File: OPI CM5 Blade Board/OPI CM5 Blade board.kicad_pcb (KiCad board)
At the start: 2 copper layers, 241.6 x 42.5 mm, 11 parts, among them J1 HIROSE_DF40C-100DS-0.4V_51_, J2 HIROSE_DF40C-100DS-0.4V_51_, J3 HIROSE_DF40C-100DS-0.4V_51_, J4 BUS_PCIexpress_x4, J5 M.2, U1 SHT4X, U5 SHT4X

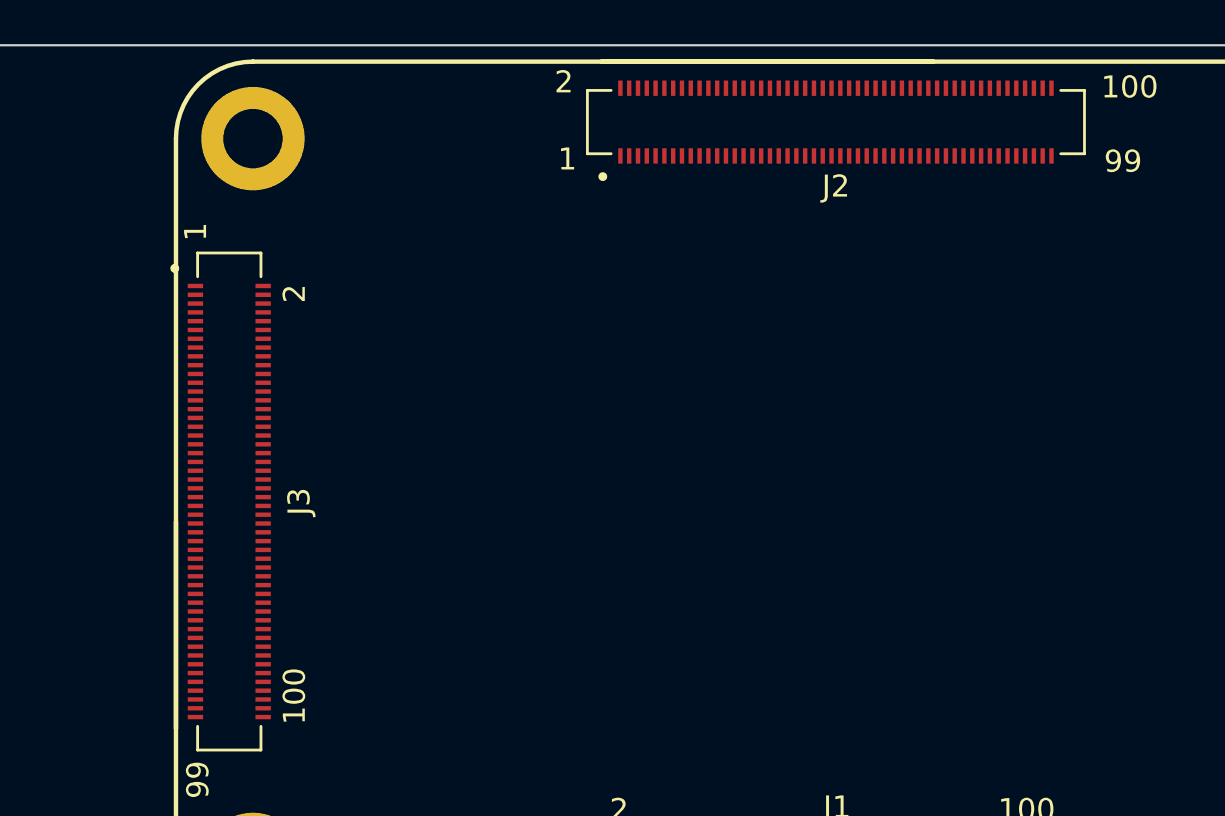
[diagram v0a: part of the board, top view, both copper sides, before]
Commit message: Working on HDMI PCIe connector wiring
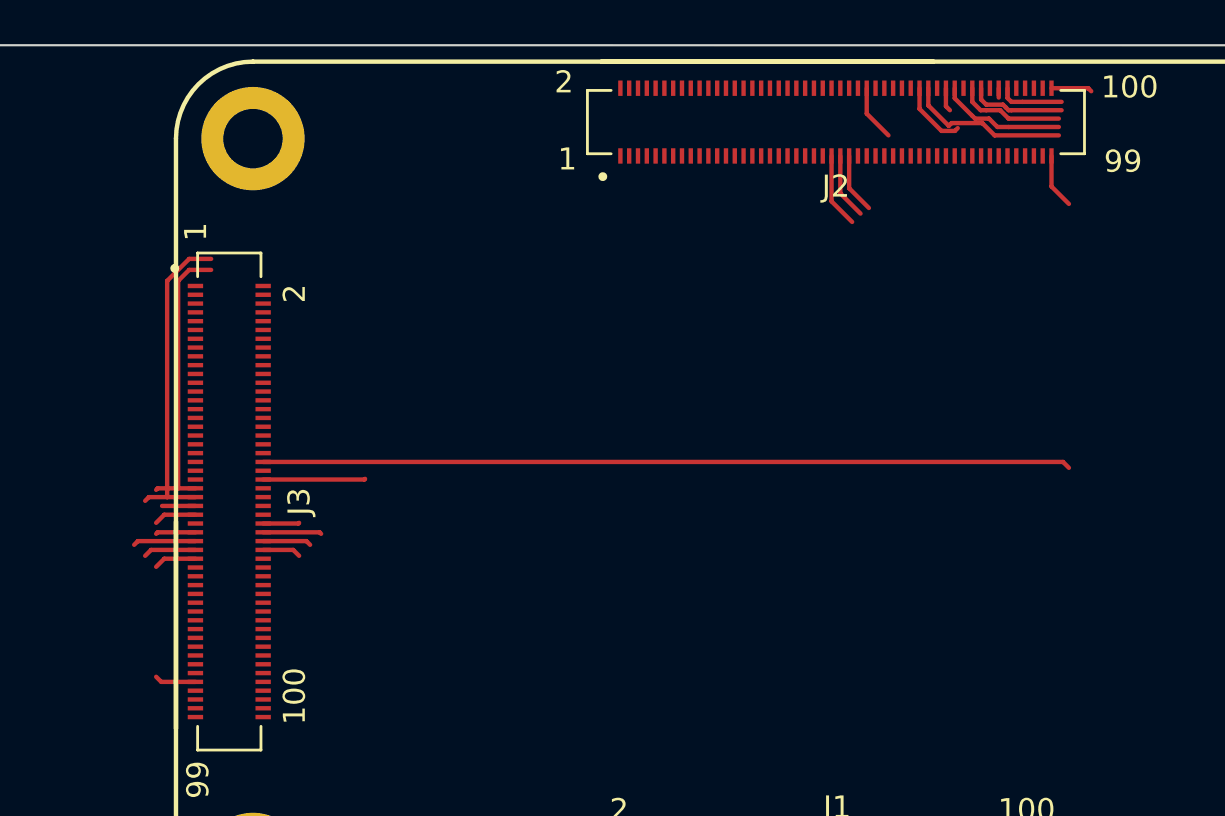
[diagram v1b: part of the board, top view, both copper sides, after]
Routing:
- net (no net): track 0.00 -> 137.6 mm
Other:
- copper layers 2 -> 4

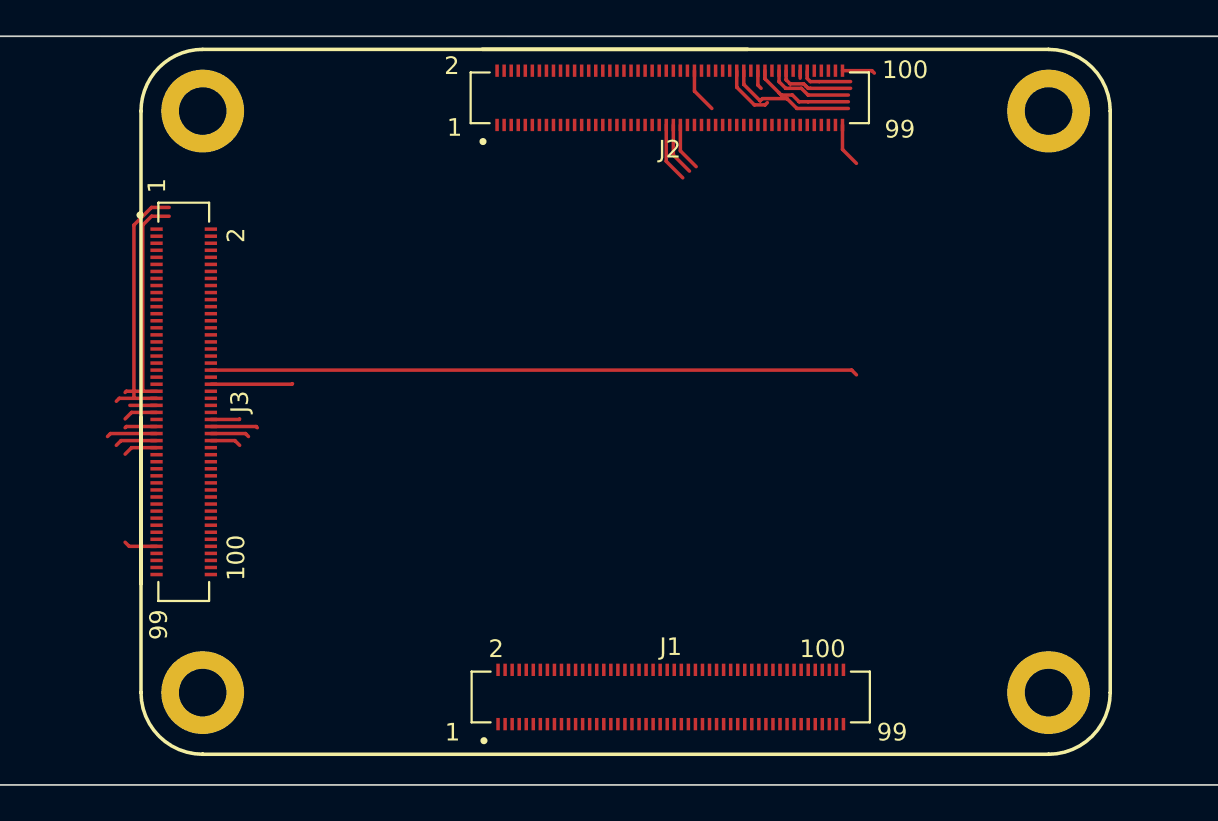
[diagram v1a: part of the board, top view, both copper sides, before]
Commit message: Working on USB differential pairs
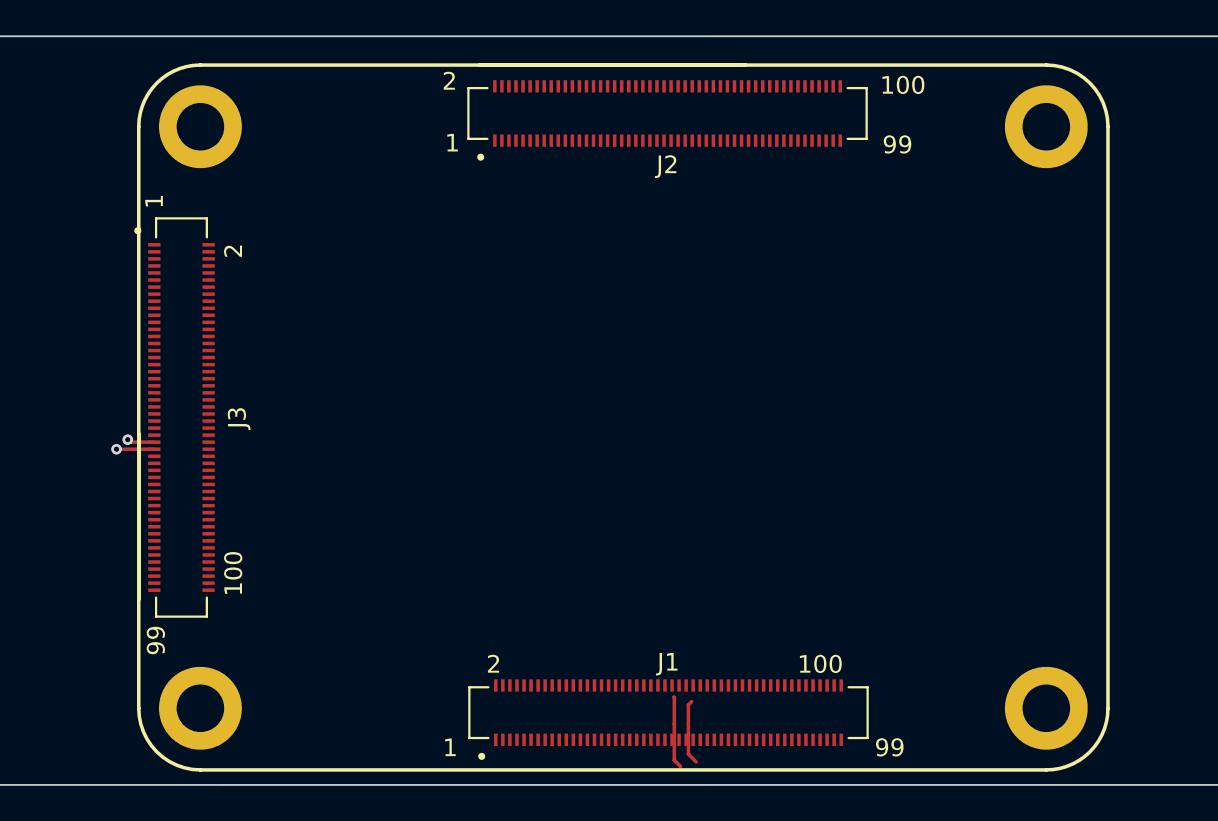
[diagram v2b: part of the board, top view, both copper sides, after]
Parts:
- moved H3 0.90 mm to (203.0, 33.3)
- moved H4 0.90 mm to (251.0, 33.3)
- moved J3 0.90 mm to (201.9, 49.8)
- moved H1 0.90 mm to (251.0, 66.3)
- moved H2 0.90 mm to (203.0, 66.3)
- moved J1 0.90 mm to (229.5, 66.5)
- moved J2 0.90 mm to (229.5, 32.5)
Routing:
- net (no net): track 137.6 -> 11.5 mm, vias 0 -> 2

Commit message: Working on M.2 SSD
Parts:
- removed U5: SHT4X, OPI_CM5_TEMP_SENSOR:SHT4X
- added D1: D5819WS, Diode_SMD:D_SOD-323, F.Cu at (174.8, 21.5)
- added D17: JEB05DFA, OPI_CM5_TVS_DIODE:DFN1006-2, F.Cu at (171.4, 18.1)
- added D2: JEB05DFA, OPI_CM5_TVS_DIODE:DFN1006-2, F.Cu at (171.4, 13.4)
- added D33: JEB05DFA, OPI_CM5_TVS_DIODE:DFN1006-2, F.Cu at (171.4, 20.5)
- added D4: JEB05DFA, OPI_CM5_TVS_DIODE:DFN1006-2, F.Cu at (171.4, 15.8)
- added ED5: ESD5341N, OPI_CM5_TVS_DIODE:DFN1006-2, F.Cu at (171.4, 22.8)
- added ED6: ESD5341N, OPI_CM5_TVS_DIODE:DFN1006-2, F.Cu at (171.4, 25.1)
- added Q1: 2SK3018, Package_TO_SOT_SMD:SOT-323_SC-70, F.Cu at (174.9, 14.3)
- added Q2: 2SK3018, Package_TO_SOT_SMD:SOT-323_SC-70, F.Cu at (174.9, 18.2)
- added U2: SHT40-BD1B-R3, OPI_CM5_TEMP_SENSOR:SHT4X, F.Cu at (174.4, 24.5)
- H1, H2, H3, H4: value MountingHole_2.7mm_M2.5_DIN965_Pad -> MountingHole_Pad
- J1: value HIROSE_DF40C-100DS-0.4V_51_ -> OPi_CM5_CORE JP1 100PIN
- J2: value HIROSE_DF40C-100DS-0.4V_51_ -> OPi_CM5_CORE JP2 100PIN
- J3: value HIROSE_DF40C-100DS-0.4V_51_ -> OPi_CM5_CORE JP13100PIN
- J4: value BUS_PCIexpress_x4 -> Bus_PCI_Express_x4
- J5: value M.2 -> J_1-2199230-5
- U1: value SHT4X -> SHT40-BD1B-R3
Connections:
- H1 pad 1: (no net) -> unconnected-(H1-Pad1)
- H2 pad 1: (no net) -> unconnected-(H2-Pad1)
- H3 pad 1: (no net) -> unconnected-(H3-Pad1)
- H4 pad 1: (no net) -> unconnected-(H4-Pad1)
- J1 pad 1: (no net) -> GND
- J1 pad 10: (no net) -> /Reserved
- J1 pad 100: (no net) -> /GPIO4_A5
- J1 pad 11: (no net) -> /Reserved
- J1 pad 12: (no net) -> /Reserved
- J1 pad 13: (no net) -> GND
- J1 pad 14: (no net) -> GND
- J1 pad 15: (no net) -> /Reserved
- J1 pad 16: (no net) -> /Reserved
- J1 pad 17: (no net) -> /Reserved
- J1 pad 18: (no net) -> /Reserved
- J1 pad 19: (no net) -> /Reserved
- J1 pad 2: (no net) -> GND
- J1 pad 20: (no net) -> /Reserved
- J1 pad 21: (no net) -> /GPIO4_A4
- J1 pad 22: (no net) -> GND
- J1 pad 23: (no net) -> GND
- J1 pad 24: (no net) -> /GPIO1_C0
- J1 pad 25: (no net) -> /GPIO1_B0
- J1 pad 26: (no net) -> /GPIO1_C1
- J1 pad 27: (no net) -> /GPIO1_B1
- J1 pad 28: (no net) -> /GPIO1_A2
- J1 pad 29: (no net) -> /GPIO1_B2
- J1 pad 3: (no net) -> /Reserved
- J1 pad 30: (no net) -> /GPIO1_A3
- J1 pad 31: (no net) -> /GPIO1_B3
- J1 pad 32: (no net) -> GND
- J1 pad 33: (no net) -> GND
- J1 pad 34: (no net) -> /GPIO1_A4
- J1 pad 35: (no net) -> /GPIO1_D6
- J1 pad 36: (no net) -> /GPIO1_D7
- J1 pad 37: (no net) -> /GPIO1_B4
- J1 pad 38: (no net) -> /GPIO1_A5
- J1 pad 39: (no net) -> /GPIO1_B5
- J1 pad 4: (no net) -> /Reserved
- J1 pad 40: (no net) -> /GPIO1_A6
- J1 pad 41: (no net) -> /GPIO1_B6
- J1 pad 42: (no net) -> GND
- J1 pad 43: (no net) -> GND
- J1 pad 44: (no net) -> /GPIO1_A7
- J1 pad 45: (no net) -> /GPIO1_B7
- J1 pad 46: (no net) -> /GPIO1_C4
- J1 pad 47: (no net) -> /GPIO0_C2
- J1 pad 48: (no net) -> /GPIO1_C6
- J1 pad 49: (no net) -> /GPIO1_D5
- J1 pad 5: (no net) -> /Reserved
- J1 pad 50: (no net) -> /GPIO1_D0
- J1 pad 51: (no net) -> /UART2_RX
- J1 pad 52: (no net) -> GND
- J1 pad 53: (no net) -> GND
- J1 pad 54: (no net) -> /GPIO1_D1
- J1 pad 55: (no net) -> /UART2_TX
- J1 pad 56: (no net) -> /GPIO1_D2
- J1 pad 57: (no net) -> /SDMMC_CLK
- J1 pad 58: (no net) -> /GPIO1_D3
- J1 pad 59: (no net) -> GND
- J1 pad 6: (no net) -> /Reserved
- J1 pad 60: (no net) -> GND
- J1 pad 61: (no net) -> /SDMMC_D3
- J1 pad 62: (no net) -> /SDMMC_CMD
- J1 pad 63: (no net) -> /SDMMC_D0
- J1 pad 64: (no net) -> /Reserved
- J1 pad 65: (no net) -> GND
- J1 pad 66: (no net) -> GND
- J1 pad 67: (no net) -> /SDMMC_D1
- J1 pad 68: (no net) -> /SARADC_IN1
- J1 pad 69: (no net) -> /SDMMC_D2
- J1 pad 7: (no net) -> GND
- J1 pad 70: (no net) -> /Reserved
- J1 pad 71: (no net) -> GND
- J1 pad 72: (no net) -> /Reserved
- J1 pad 73: (no net) -> /Reserved
- J1 pad 74: (no net) -> GND
- J1 pad 75: (no net) -> /SDMMC_PWREN
- J1 pad 76: (no net) -> /GPIO0_A4
- J1 pad 77: (no net) -> /VBUS
- J1 pad 78: (no net) -> /GPIO_VREF
- J1 pad 79: (no net) -> /VBUS
- J1 pad 8: (no net) -> GND
- J1 pad 80: (no net) -> /I2C6_SCL_M3
- J1 pad 81: (no net) -> /VBUS
- J1 pad 82: (no net) -> /I2C6_SDA_M3
- J1 pad 83: (no net) -> /VBUS
- J1 pad 84: (no net) -> /VCC_3V3_S3
- J1 pad 85: (no net) -> /VBUS
- J1 pad 86: (no net) -> /VCC_3V3_S3
- J1 pad 87: (no net) -> /VBUS
- J1 pad 88: (no net) -> /VCC_1V8_S3
- J1 pad 89: (no net) -> /Reserved
- J1 pad 9: (no net) -> /Reserved
- J1 pad 90: (no net) -> /VCC_1V8_S3
- J1 pad 91: (no net) -> /Reserved
- J1 pad 92: (no net) -> /PMIC_RESET_L
- J1 pad 93: (no net) -> /SARADC_IN0
- J1 pad 94: (no net) -> /SARADC_IN3
- J1 pad 95: (no net) -> /GPIO4_B6
- J1 pad 96: (no net) -> /SARADC_IN2
- J1 pad 97: (no net) -> /GPIO4_A7
- J1 pad 98: (no net) -> GND
- J1 pad 99: (no net) -> /PWRON_L
- J2 pad 1: (no net) -> /TYPEC0_USB20_OTG_ID
- J2 pad 10: (no net) -> /PCIE20_2_REFCLKP
- J2 pad 100: (no net) -> /HDMI_TX0_SCL_M0
- J2 pad 11: (no net) -> /Reserved
- J2 pad 12: (no net) -> /PCIE20_2_REFCLKN
- J2 pad 13: (no net) -> GND
- J2 pad 14: (no net) -> GND
- J2 pad 15: (no net) -> /MIPI_CSI0_D0N
- J2 pad 16: (no net) -> /PCIE20_2_RXP/SATA30_2_RXP
- J2 pad 17: (no net) -> /MIPI_CSI0_D0P
- J2 pad 18: (no net) -> /PCIE20_2_RXN/SATA30_2_RXN
- J2 pad 19: (no net) -> GND
- J2 pad 2: (no net) -> /GPIO1_A0
- J2 pad 20: (no net) -> GND
- J2 pad 21: (no net) -> /MIPI_CSI0_D1N
- J2 pad 22: (no net) -> /PCIE20_2_TXP/SATA30_2_TXP
- J2 pad 23: (no net) -> /MIPI_CSI0_D1P
- J2 pad 24: (no net) -> /PCIE20_2_TXN/SATA30_2_TXN
- J2 pad 25: (no net) -> GND
- J2 pad 26: (no net) -> GND
- J2 pad 27: (no net) -> /MIPI_CSI0_CLK0N
- J2 pad 28: (no net) -> /MIPI_DPHY0_RX_D0N
- J2 pad 29: (no net) -> /MIPI_CSI0_CLK0P
- J2 pad 3: (no net) -> /TYPEC0_USB20_OTG_DM
- J2 pad 30: (no net) -> /MIPI_DPHY0_RX_D0P
- J2 pad 31: (no net) -> GND
- J2 pad 32: (no net) -> GND
- J2 pad 33: (no net) -> /MIPI_CSI0_D2N
- J2 pad 34: (no net) -> /MIPI_DPHY0_RX_D1N
- J2 pad 35: (no net) -> /MIPI_CSI0_D2N
- J2 pad 36: (no net) -> /MIPI_DPHY0_RX_D1P
- J2 pad 37: (no net) -> GND
- J2 pad 38: (no net) -> GND
- J2 pad 39: (no net) -> /MIPI_CSI0_D3N
- J2 pad 4: (no net) -> /GPIO1_A1
- J2 pad 40: (no net) -> /MIPI_DPHY0_RX_CLKN
- J2 pad 41: (no net) -> /MIPI_CSI0_D3P
- J2 pad 42: (no net) -> /MIPI_DPHY0_RX_CLKP
- J2 pad 43: (no net) -> GND
- J2 pad 44: (no net) -> GND
- J2 pad 45: (no net) -> /MIPI_CSI0_CLK1N
- J2 pad 46: (no net) -> /Reserved
- J2 pad 47: (no net) -> /MIPI_CSI0_CLK1P
- J2 pad 48: (no net) -> /Reserved
- J2 pad 49: (no net) -> /HDMI0_TX_ON_H
- J2 pad 5: (no net) -> /TYPEC0_USB20_OTG_DP
- J2 pad 50: (no net) -> GND
- J2 pad 51: (no net) -> /HDMI_TX0_CEC_M0
- J2 pad 52: (no net) -> /Reserved
- J2 pad 53: (no net) -> /HDMI_TX0_SBDN
- J2 pad 54: (no net) -> /Reserved
- J2 pad 55: (no net) -> GND
- J2 pad 56: (no net) -> GND
- J2 pad 57: (no net) -> /MIPI_DPHY0_TX_D0N
- J2 pad 58: (no net) -> /HDMI0_SBDP
- J2 pad 59: (no net) -> /MIPI_DPHY0_TX_D0P
- J2 pad 6: (no net) -> /GPIO4_A6
- J2 pad 60: (no net) -> /Reserved
- J2 pad 61: (no net) -> GND
- J2 pad 62: (no net) -> GND
- J2 pad 63: (no net) -> /MIPI_DPHY0_TX_D1N
- J2 pad 64: (no net) -> /Reserved
- J2 pad 65: (no net) -> /MIPI_DPHY0_TX_D1P
- J2 pad 66: (no net) -> /Reserved
- J2 pad 67: (no net) -> GND
- J2 pad 68: (no net) -> GND
- J2 pad 69: (no net) -> /MIPI_DPHY0_TX_CLKN
- J2 pad 7: (no net) -> GND
- J2 pad 70: (no net) -> /HDMI_TX0_D2P
- J2 pad 71: (no net) -> /MIPI_DPHY0_TX_CLKP
- J2 pad 72: (no net) -> /HDMI_TX0_D2N
- J2 pad 73: (no net) -> GND
- J2 pad 74: (no net) -> GND
- J2 pad 75: (no net) -> /MIPI_DPHY1_TX_D0N
- J2 pad 76: (no net) -> /HDMI_TX0_D1P
- J2 pad 77: (no net) -> /MIPI_DPHY1_TX_D0P
- J2 pad 78: (no net) -> /HDMI_TX0_D1N
- J2 pad 79: (no net) -> GND
- J2 pad 8: (no net) -> GND
- J2 pad 80: (no net) -> GND
- J2 pad 81: (no net) -> /MIPI_DPHY1_TX_D1N
- J2 pad 82: (no net) -> /HDMI_TX0_D0P
- J2 pad 83: (no net) -> /MIPI_DPHY1_TX_D1P
- J2 pad 84: (no net) -> /HDMI_TX0_D0N
- J2 pad 85: (no net) -> GND
- J2 pad 86: (no net) -> GND
- J2 pad 87: (no net) -> /MIPI_DPHY1_TX_CLKN
- J2 pad 88: (no net) -> /HDMI_TX0_D3P
- J2 pad 89: (no net) -> /MIPI_DPHY1_TX_CLKP
- J2 pad 9: (no net) -> /GPIO4_A2
- J2 pad 90: (no net) -> /HDMI_TX0_D3N
- J2 pad 91: (no net) -> GND
- J2 pad 92: (no net) -> GND
- J2 pad 93: (no net) -> /MIPI_DPHY1_TX_D2N
- J2 pad 94: (no net) -> /MIPI_DPHY1_TX_D3N
- J2 pad 95: (no net) -> /MIPI_DPHY1_TX_D2P
- J2 pad 96: (no net) -> /MIPI_DPHY1_TX_D3P
- J2 pad 97: (no net) -> GND
- J2 pad 98: (no net) -> GND
- J2 pad 99: (no net) -> /HDMI_TX0_SDA_M0
- J3 pad 1: (no net) -> /USB20_HOST1_DP
- J3 pad 10: (no net) -> /TYPEC0_SSRX2N
- J3 pad 100: (no net) -> GND
- J3 pad 11: (no net) -> GND
- J3 pad 12: (no net) -> GND
- J3 pad 13: (no net) -> /USB20_HOST0_DP
- J3 pad 14: (no net) -> /TYPEC0_SSTX1N
- J3 pad 15: (no net) -> /USB20_HOST0_DM
- J3 pad 16: (no net) -> /TYPEC0_SSTX1P
- J3 pad 17: (no net) -> GND
- J3 pad 18: (no net) -> GND
- J3 pad 19: (no net) -> /TYPEC0_SSRX1P
- J3 pad 2: (no net) -> /TYPEC0_SSTX2P
- J3 pad 20: (no net) -> /GPIO3_C6
- J3 pad 21: (no net) -> /TYPEC0_SSRX1P
- J3 pad 22: (no net) -> /PCIE20x1_2_CLKREQn_M0
- J3 pad 23: (no net) -> GND
- J3 pad 24: (no net) -> /PCIE20x1_2_PERSTn_M0
- J3 pad 25: (no net) -> /MIPI_DPHY1_RX_CLKP
- J3 pad 26: (no net) -> /GPIO3_D5
- J3 pad 27: (no net) -> /MIPI_DPHY1_RX_CLKN
- J3 pad 28: (no net) -> /GPIO3_D2
- J3 pad 29: (no net) -> GND
- J3 pad 3: (no net) -> /USB20_HOST1_DN
- J3 pad 30: (no net) -> /GPIO3_D4
- J3 pad 31: (no net) -> /MIPI_DPHY1_RX_D1P
- J3 pad 32: (no net) -> GND
- J3 pad 33: (no net) -> /MIPI_DPHY1_RX_D1N
- J3 pad 34: (no net) -> /GPIO3_B7
- J3 pad 35: (no net) -> GND
- J3 pad 36: (no net) -> /GPIO3_C5
- J3 pad 37: (no net) -> /MIPI_DPHY1_RX_D0P
- J3 pad 38: (no net) -> /GPIO3_C4
- J3 pad 39: (no net) -> /MIPI_DPHY1_RX_D0N
- J3 pad 4: (no net) -> /TYPEC0_SSTX2N
- J3 pad 40: (no net) -> /GPIO3_D3
- J3 pad 41: (no net) -> GND
- J3 pad 42: (no net) -> /GMAC_TXD3
- J3 pad 43: (no net) -> /PCIE20x1_2_WAKEn_M0
- J3 pad 44: (no net) -> GND
- J3 pad 45: (no net) -> GND
- J3 pad 46: (no net) -> /GMAC_TXD0
- J3 pad 47: (no net) -> /GMAC_TXD2
- J3 pad 48: (no net) -> /GPIO3_B2
- J3 pad 49: (no net) -> /GMAC_TXD1
- J3 pad 5: (no net) -> GND
- J3 pad 50: (no net) -> /GPIO3_C1
- J3 pad 51: (no net) -> /GMAC_TXEN
- J3 pad 52: (no net) -> /GPIO3_A6
- J3 pad 53: (no net) -> /GMAC_MDIO
- J3 pad 54: (no net) -> GND
- J3 pad 55: (no net) -> GND
- J3 pad 56: (no net) -> /GMAC_RXD1
- J3 pad 57: (no net) -> /GMAC_MCLK/PWM13
- J3 pad 58: (no net) -> /GMAC_RXCLK
- J3 pad 59: (no net) -> /GMAC_RXDV
- J3 pad 6: (no net) -> GND
- J3 pad 60: (no net) -> /GMAC_RXD0
- J3 pad 61: (no net) -> /GMAC_RXD2
- J3 pad 62: (no net) -> /GMAC_TXCLK
- J3 pad 63: (no net) -> /GMAC_RXD3
- J3 pad 64: (no net) -> GND
- J3 pad 65: (no net) -> GND
- J3 pad 66: (no net) -> /GPIO0_B0
- J3 pad 67: (no net) -> /GPIO0_A0
- J3 pad 68: (no net) -> /I2S0_MCLK
- J3 pad 69: (no net) -> /GPIO1_C2
- J3 pad 7: (no net) -> /TYPEC0_SBU1
- J3 pad 70: (no net) -> /I2S0_SDO0
- J3 pad 71: (no net) -> /GPIO1_C5
- J3 pad 72: (no net) -> /GPIO3_C0
- J3 pad 73: (no net) -> /GPIO1_D4
- J3 pad 74: (no net) -> GND
- J3 pad 75: (no net) -> GND
- J3 pad 76: (no net) -> /PCIE20_0_REFCLKP
- J3 pad 77: (no net) -> /GPIO0_D5
- J3 pad 78: (no net) -> /PCIE20_0_REFCLKN
- J3 pad 79: (no net) -> /GPIO0_C7
- J3 pad 8: (no net) -> /TYPEC0_SSRX2P
- J3 pad 80: (no net) -> GND
- J3 pad 81: (no net) -> /GPIO0_D4
- J3 pad 82: (no net) -> /PCIE20_0_TXP
- J3 pad 83: (no net) -> /GPIO0_C4
- J3 pad 84: (no net) -> /PCIE20_0_TXN
- J3 pad 85: (no net) -> /GPIO0_D3
- J3 pad 86: (no net) -> GND
- J3 pad 87: (no net) -> GND
- J3 pad 88: (no net) -> /PCIE20_0_RXN
- J3 pad 89: (no net) -> /GPIO0_D0
- J3 pad 9: (no net) -> /TYPEC0_SBU2
- J3 pad 90: (no net) -> /PCIE20_0_RXP
- J3 pad 91: (no net) -> /GMAC_MDC
- J3 pad 92: (no net) -> GND
- J3 pad 93: (no net) -> /GPIO4_A3
- J3 pad 94: (no net) -> /GPIO0_C5
- J3 pad 95: (no net) -> /GPIO4_B3
- J3 pad 96: (no net) -> /GPIO0_B2
- J3 pad 97: (no net) -> /GPIO4_B2
- J3 pad 98: (no net) -> /GPIO0_C6
- J3 pad 99: (no net) -> GND
- J4 pad A1: (no net) -> unconnected-(J4-~{PRSNT1}-PadA1)
- J4 pad A10: (no net) -> Net-(J4-+3.3V-PadA10)
- J4 pad A11: (no net) -> unconnected-(J4-~{PERST}-PadA11)
- J4 pad A12: (no net) -> Net-(J4-GND-PadA12)
- J4 pad A13: (no net) -> unconnected-(J4-REFCLK+-PadA13)
- J4 pad A14: (no net) -> unconnected-(J4-REFCLK--PadA14)
- J4 pad A15: (no net) -> Net-(J4-GND-PadA12)
- J4 pad A16: (no net) -> unconnected-(J4-PERp0-PadA16)
- J4 pad A17: (no net) -> unconnected-(J4-PERn0-PadA17)
- J4 pad A18: (no net) -> Net-(J4-GND-PadA12)
- J4 pad A19: (no net) -> unconnected-(J4-RSVD-PadA19)
- J4 pad A2: (no net) -> Net-(J4-+12V-PadA2)
- J4 pad A20: (no net) -> Net-(J4-GND-PadA12)
- J4 pad A21: (no net) -> unconnected-(J4-PERp1-PadA21)
- J4 pad A22: (no net) -> unconnected-(J4-PERn1-PadA22)
- J4 pad A23: (no net) -> Net-(J4-GND-PadA12)
- J4 pad A24: (no net) -> Net-(J4-GND-PadA12)
- J4 pad A25: (no net) -> unconnected-(J4-PERp2-PadA25)
- J4 pad A26: (no net) -> unconnected-(J4-PERn2-PadA26)
- J4 pad A27: (no net) -> Net-(J4-GND-PadA12)
- J4 pad A28: (no net) -> Net-(J4-GND-PadA12)
- J4 pad A29: (no net) -> unconnected-(J4-PERp3-PadA29)
- J4 pad A3: (no net) -> Net-(J4-+12V-PadA2)
- J4 pad A30: (no net) -> unconnected-(J4-PERn3-PadA30)
- J4 pad A31: (no net) -> Net-(J4-GND-PadA12)
- J4 pad A32: (no net) -> unconnected-(J4-RSVD-PadA32)
- J4 pad A4: (no net) -> Net-(J4-GND-PadA12)
- J4 pad A5: (no net) -> unconnected-(J4-JTAG2-PadA5)
- J4 pad A6: (no net) -> unconnected-(J4-JTAG3-PadA6)
- J4 pad A7: (no net) -> unconnected-(J4-JTAG4-PadA7)
- J4 pad A8: (no net) -> unconnected-(J4-JTAG5-PadA8)
- J4 pad A9: (no net) -> Net-(J4-+3.3V-PadA10)
- J4 pad B1: (no net) -> Net-(J4-+12V-PadA2)
- J4 pad B10: (no net) -> unconnected-(J4-3.3Vaux-PadB10)
- J4 pad B11: (no net) -> unconnected-(J4-~{WAKE}-PadB11)
- J4 pad B12: (no net) -> unconnected-(J4-RSVD-PadB12)
- J4 pad B13: (no net) -> Net-(J4-GND-PadA12)
- J4 pad B14: (no net) -> /USB20_HOST1_DP
- J4 pad B15: (no net) -> /USB20_HOST1_DN
- J4 pad B16: (no net) -> Net-(J4-GND-PadA12)
- J4 pad B17: (no net) -> unconnected-(J4-~{PRSNT2}-PadB17)
- J4 pad B18: (no net) -> Net-(J4-GND-PadA12)
- J4 pad B19: (no net) -> unconnected-(J4-PETp1-PadB19)
- J4 pad B2: (no net) -> Net-(J4-+12V-PadA2)
- J4 pad B20: (no net) -> unconnected-(J4-PETn1-PadB20)
- J4 pad B21: (no net) -> Net-(J4-GND-PadA12)
- J4 pad B22: (no net) -> Net-(J4-GND-PadA12)
- J4 pad B23: (no net) -> unconnected-(J4-PETp2-PadB23)
- J4 pad B24: (no net) -> unconnected-(J4-PETn2-PadB24)
- J4 pad B25: (no net) -> Net-(J4-GND-PadA12)
- J4 pad B26: (no net) -> Net-(J4-GND-PadA12)
- J4 pad B27: (no net) -> unconnected-(J4-PETp3-PadB27)
- J4 pad B28: (no net) -> unconnected-(J4-PETn3-PadB28)
- J4 pad B29: (no net) -> Net-(J4-GND-PadA12)
- J4 pad B3: (no net) -> Net-(J4-+12V-PadA2)
- J4 pad B30: (no net) -> unconnected-(J4-RSVD-PadB30)
- J4 pad B31: (no net) -> unconnected-(J4-~{PRSNT2}-PadB31)
- J4 pad B32: (no net) -> Net-(J4-GND-PadA12)
- J4 pad B4: (no net) -> Net-(J4-GND-PadA12)
- J4 pad B5: (no net) -> unconnected-(J4-SMCLK-PadB5)
- J4 pad B6: (no net) -> unconnected-(J4-SMDAT-PadB6)
- J4 pad B7: (no net) -> Net-(J4-GND-PadA12)
- J4 pad B8: (no net) -> Net-(J4-+3.3V-PadA10)
- J4 pad B9: (no net) -> unconnected-(J4-JTAG1-PadB9)
- J5 pad 1: (no net) -> unconnected-(J5-CONFIG_3-Pad1)
- J5 pad 10: (no net) -> unconnected-(J5-DAS/DSS-Pad10)
- J5 pad 11: (no net) -> unconnected-(J5-PETN3-Pad11)
- J5 pad 12: (no net) -> unconnected-(J5-VCC_3.3-Pad12)
- J5 pad 13: (no net) -> unconnected-(J5-PETP3-Pad13)
- J5 pad 14: (no net) -> unconnected-(J5-VCC_3.3-Pad14)
- J5 pad 15: (no net) -> unconnected-(J5-GND-Pad15)
- J5 pad 16: (no net) -> unconnected-(J5-VCC_3.3-Pad16)
- J5 pad 17: (no net) -> unconnected-(J5-PERN2-Pad17)
- J5 pad 18: (no net) -> unconnected-(J5-VCC_3.3-Pad18)
- J5 pad 19: (no net) -> unconnected-(J5-PERP2-Pad19)
- J5 pad 2: (no net) -> unconnected-(J5-VCC_3.3-Pad2)
- J5 pad 20: (no net) -> unconnected-(J5-N/A-Pad20)
- J5 pad 21: (no net) -> unconnected-(J5-CONFIG_0-Pad21)
- J5 pad 22: (no net) -> unconnected-(J5-N/A-Pad22)
- J5 pad 23: (no net) -> unconnected-(J5-PETN2-Pad23)
- J5 pad 24: (no net) -> unconnected-(J5-N/A-Pad24)
- J5 pad 25: (no net) -> unconnected-(J5-PETP2-Pad25)
- J5 pad 26: (no net) -> unconnected-(J5-N/A-Pad26)
- J5 pad 27: (no net) -> unconnected-(J5-GND-Pad27)
- J5 pad 28: (no net) -> unconnected-(J5-N/A-Pad28)
- J5 pad 29: (no net) -> unconnected-(J5-PERN1-Pad29)
- J5 pad 3: (no net) -> unconnected-(J5-GND-Pad3)
- J5 pad 30: (no net) -> unconnected-(J5-N/A-Pad30)
- J5 pad 31: (no net) -> unconnected-(J5-PERP1-Pad31)
- J5 pad 32: (no net) -> unconnected-(J5-N/A-Pad32)
- J5 pad 33: (no net) -> unconnected-(J5-GND-Pad33)
- J5 pad 34: (no net) -> unconnected-(J5-N/A-Pad34)
- J5 pad 35: (no net) -> unconnected-(J5-PETN1-Pad35)
- J5 pad 36: (no net) -> unconnected-(J5-N/A-Pad36)
- J5 pad 37: (no net) -> unconnected-(J5-PETP1-Pad37)
- J5 pad 38: (no net) -> unconnected-(J5-DEVSLP-Pad38)
- J5 pad 39: (no net) -> unconnected-(J5-GND-Pad39)
- J5 pad 4: (no net) -> unconnected-(J5-VCC_3.3-Pad4)
- J5 pad 40: (no net) -> unconnected-(J5-N/A-Pad40)
- J5 pad 41: (no net) -> unconnected-(J5-SATA_B+/PERN0-Pad41)
- J5 pad 42: (no net) -> unconnected-(J5-N/A-Pad42)
- J5 pad 43: (no net) -> unconnected-(J5-SATA_B-/PERP0-Pad43)
- J5 pad 44: (no net) -> unconnected-(J5-N/A-Pad44)
- J5 pad 45: (no net) -> unconnected-(J5-GND-Pad45)
- J5 pad 46: (no net) -> unconnected-(J5-N/A-Pad46)
- J5 pad 47: (no net) -> unconnected-(J5-SATA_A-/PETN0-Pad47)
- J5 pad 48: (no net) -> unconnected-(J5-N/A-Pad48)
- J5 pad 49: (no net) -> unconnected-(J5-SATA_A+/PETP0-Pad49)
- J5 pad 5: (no net) -> unconnected-(J5-PERN3-Pad5)
- J5 pad 50: (no net) -> unconnected-(J5-~{PERST}-Pad50)
- J5 pad 51: (no net) -> unconnected-(J5-GND-Pad51)
- J5 pad 52: (no net) -> unconnected-(J5-~{CLKREQ}-Pad52)
- J5 pad 53: (no net) -> unconnected-(J5-REFCLKN-Pad53)
- J5 pad 54: (no net) -> unconnected-(J5-~{PEWAKE}-Pad54)
- J5 pad 55: (no net) -> unconnected-(J5-REFCLKP-Pad55)
- J5 pad 56: (no net) -> unconnected-(J5-MFG1-Pad56)
- J5 pad 57: (no net) -> Net-(J5-GND-Pad57)
- J5 pad 58: (no net) -> unconnected-(J5-MFG2-Pad58)
- J5 pad 6: (no net) -> unconnected-(J5-N/A-Pad6)
- J5 pad 67: (no net) -> unconnected-(J5-N/A-Pad67)
- J5 pad 68: (no net) -> unconnected-(J5-SUSCLK-Pad68)
- J5 pad 69: (no net) -> unconnected-(J5-CONFIG_1-Pad69)
- J5 pad 7: (no net) -> unconnected-(J5-PERP3-Pad7)
- J5 pad 70: (no net) -> unconnected-(J5-VCC_3.3-Pad70)
- J5 pad 71: (no net) -> unconnected-(J5-GND-Pad71)
- J5 pad 72: (no net) -> unconnected-(J5-VCC_3.3-Pad72)
- J5 pad 73: (no net) -> unconnected-(J5-GND-Pad73)
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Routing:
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
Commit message: Working on routing
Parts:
- removed D1: D5819WS, Diode_SMD:D_SOD-323
- removed Q1, Q2: 2SK3018, Package_TO_SOT_SMD:SOT-323_SC-70
- added C10: 100nF, Capacitor_SMD:C_0201_0603Metric_Pad0.64x0.40mm_HandSolder, F.Cu at (168.3, 47.5)
- added C11: 100nF, Capacitor_SMD:C_0201_0603Metric_Pad0.64x0.40mm_HandSolder, F.Cu at (168.3, 46.5)
- added C12: 10μF, Capacitor_SMD:C_0805_2012Metric_Pad1.18x1.45mm_HandSolder, F.Cu at (173.4, 30.5)
- added C13: 22μF, Capacitor_SMD:C_0805_2012Metric_Pad1.18x1.45mm_HandSolder, F.Cu at (173.4, 33.0)
- added C14: 10μF, Capacitor_SMD:C_0805_2012Metric_Pad1.18x1.45mm_HandSolder, F.Cu at (181.3, 40.6)
- added C15: 10μF, Capacitor_SMD:C_0805_2012Metric_Pad1.18x1.45mm_HandSolder, F.Cu at (264.4, 66.5)
- added C16: 100nF, Capacitor_SMD:C_0201_0603Metric_Pad0.64x0.40mm_HandSolder, F.Cu at (260.3, 63.0)
- added C17: 22pF, Capacitor_SMD:C_0201_0603Metric_Pad0.64x0.40mm_HandSolder, F.Cu at (265.9, 55.6)
- added C18: 47μF, Capacitor_SMD:C_0805_2012Metric_Pad1.18x1.45mm_HandSolder, F.Cu at (256.3, 66.5)
- added C19: 22μF, Capacitor_SMD:C_0805_2012Metric_Pad1.18x1.45mm_HandSolder, F.Cu at (256.3, 56.1)
- added C20: 10μF, Capacitor_SMD:C_0805_2012Metric_Pad1.18x1.45mm_HandSolder, F.Cu at (256.3, 58.6)
- added C27: 100nF, Capacitor_SMD:C_0201_0603Metric_Pad0.64x0.40mm_HandSolder, F.Cu at (47.2, 44.7)
- added C3: 100nF, Capacitor_SMD:C_0201_0603Metric_Pad0.64x0.40mm_HandSolder, F.Cu at (47.2, 51.1)
- added C40: 47μF, Capacitor_SMD:C_0805_2012Metric_Pad1.18x1.45mm_HandSolder, F.Cu at (157.4, 58.4)
- added C43: 47μF, Capacitor_SMD:C_0805_2012Metric_Pad1.18x1.45mm_HandSolder, F.Cu at (157.4, 30.2)
- added C6: 100nF, Capacitor_SMD:C_0201_0603Metric_Pad0.64x0.40mm_HandSolder, F.Cu at (47.2, 38.4)
- added C7: 100nF, Capacitor_SMD:C_0201_0603Metric_Pad0.64x0.40mm_HandSolder, F.Cu at (177.3, 37.3)
- added C8: 22pF, Capacitor_SMD:C_0201_0603Metric_Pad0.64x0.40mm_HandSolder, F.Cu at (182.8, 30.2)
- added C9: 47μF, Capacitor_SMD:C_0805_2012Metric_Pad1.18x1.45mm_HandSolder, F.Cu at (173.4, 40.6)
- added CC1: 100nF, Capacitor_SMD:C_0201_0603Metric_Pad0.64x0.40mm_HandSolder, F.Cu at (47.2, 32.0)
- added CC2: 100nF, Capacitor_SMD:C_0201_0603Metric_Pad0.64x0.40mm_HandSolder, F.Cu at (173.4, 42.4)
- added CC3: 100nF, Capacitor_SMD:C_0201_0603Metric_Pad0.64x0.40mm_HandSolder, F.Cu at (179.8, 32.3)
- added CC4: 100nF, Capacitor_SMD:C_0201_0603Metric_Pad0.64x0.40mm_HandSolder, F.Cu at (181.3, 42.4)
- added CC5: 100nF, Capacitor_SMD:C_0201_0603Metric_Pad0.64x0.40mm_HandSolder, F.Cu at (264.4, 68.8)
- added CC6: 100nF, Capacitor_SMD:C_0201_0603Metric_Pad0.64x0.40mm_HandSolder, F.Cu at (262.9, 57.4)
- added CC7: 100nF, Capacitor_SMD:C_0201_0603Metric_Pad0.64x0.40mm_HandSolder, F.Cu at (256.3, 68.8)
- added D10: YLO, LED_SMD:LED_0603_1608Metric_Pad1.05x0.95mm_HandSolder, F.Cu at (39.6, 65.1)
- added D11: BLU, LED_SMD:LED_0603_1608Metric_Pad1.05x0.95mm_HandSolder, F.Cu at (39.6, 67.7)
- added D3: RED, LED_SMD:LED_0603_1608Metric_Pad1.05x0.95mm_HandSolder, F.Cu at (39.6, 54.8)
- added D7: ORN, LED_SMD:LED_0603_1608Metric_Pad1.05x0.95mm_HandSolder, F.Cu at (39.6, 57.4)
- added D8: GRN, LED_SMD:LED_0603_1608Metric_Pad1.05x0.95mm_HandSolder, F.Cu at (39.6, 59.9)
- added D9: YLO, LED_SMD:LED_0603_1608Metric_Pad1.05x0.95mm_HandSolder, F.Cu at (39.6, 62.5)
- added L1: WPN4020H2R2MT, OPI_CM5_INDUCTOR_SMD:WPN4020H2R2MT, F.Cu at (173.4, 36.8)
- added L2: WPN4020H2R2MT, OPI_CM5_INDUCTOR_SMD:WPN4020H2R2MT, F.Cu at (256.3, 62.5)
- added NC/SIP1X3: SIP1X3, Connector_PinHeader_1.00mm:PinHeader_1x03_P1.00mm_Vertical_SMD_Pin1Right, F.Cu at (66.3, 62.2)
- added R10: 470R, Resistor_SMD:R_0201_0603Metric_Pad0.64x0.40mm_HandSolder, F.Cu at (43.4, 65.1)
- added R11: 0R, Resistor_SMD:R_0201_0603Metric_Pad0.64x0.40mm_HandSolder, F.Cu at (64.9, 65.6)
- added R12: 0R, Resistor_SMD:R_0201_0603Metric_Pad0.64x0.40mm_HandSolder, F.Cu at (64.9, 67.4)
- added R13: 470R, Resistor_SMD:R_0201_0603Metric_Pad0.64x0.40mm_HandSolder, F.Cu at (43.2, 67.7)
- added R139: 100R, Resistor_SMD:R_0201_0603Metric_Pad0.64x0.40mm_HandSolder, F.Cu at (48.5, 51.1)
- added R14: 100R, Resistor_SMD:R_0201_0603Metric_Pad0.64x0.40mm_HandSolder, F.Cu at (48.5, 38.4)
- added R144: 200R, Resistor_SMD:R_0201_0603Metric_Pad0.64x0.40mm_HandSolder, F.Cu at (48.5, 44.7)
- added R18: 100K, Resistor_SMD:R_0201_0603Metric_Pad0.64x0.40mm_HandSolder, F.Cu at (179.8, 34.3)
- added R2: 200R, Resistor_SMD:R_0201_0603Metric_Pad0.64x0.40mm_HandSolder, F.Cu at (48.5, 32.0)
- added R20: 100K, Resistor_SMD:R_0201_0603Metric_Pad0.64x0.40mm_HandSolder, F.Cu at (179.8, 30.2)
- added R21: 100K, Resistor_SMD:R_0201_0603Metric_Pad0.64x0.40mm_HandSolder, F.Cu at (262.9, 59.2)
- added R22: 100K, Resistor_SMD:R_0201_0603Metric_Pad0.64x0.40mm_HandSolder, F.Cu at (262.9, 55.6)
- added R23: 4K7, Resistor_SMD:R_0201_0603Metric_Pad0.64x0.40mm_HandSolder, F.Cu at (151.8, 58.4)
- added R24: 4K7, Resistor_SMD:R_0201_0603Metric_Pad0.64x0.40mm_HandSolder, F.Cu at (152.8, 58.4)
- added R25: 4K7, Resistor_SMD:R_0201_0603Metric_Pad0.64x0.40mm_HandSolder, F.Cu at (153.8, 58.4)
- added R26: 110K, Resistor_SMD:R_0201_0603Metric_Pad0.64x0.40mm_HandSolder, F.Cu at (265.9, 57.4)
- added R27: 15K, Resistor_SMD:R_0201_0603Metric_Pad0.64x0.40mm_HandSolder, F.Cu at (265.9, 59.2)
- added R3: 560R, Resistor_SMD:R_0201_0603Metric_Pad0.64x0.40mm_HandSolder, F.Cu at (43.2, 54.8)
- added R4: 100K, Resistor_SMD:R_0201_0603Metric_Pad0.64x0.40mm_HandSolder, F.Cu at (182.8, 32.3)
- added R5: 22.1K, Resistor_SMD:R_0201_0603Metric_Pad0.64x0.40mm_HandSolder, F.Cu at (182.8, 34.3)
- added R6: 470R, Resistor_SMD:R_0201_0603Metric_Pad0.64x0.40mm_HandSolder, F.Cu at (43.2, 57.4)
- added R7: 470R, Resistor_SMD:R_0201_0603Metric_Pad0.64x0.40mm_HandSolder, F.Cu at (43.2, 59.9)
- added R8: 470R, Resistor_SMD:R_0201_0603Metric_Pad0.64x0.40mm_HandSolder, F.Cu at (43.2, 62.5)
- added SW1: USER_SW, OPI_CM5_PUSH_SW:SW4_PTS815 SJM 250 SMTR LFS_CNK, F.Cu at (40.9, 44.7)
- added SW2: RESET_SW, OPI_CM5_PUSH_SW:SW4_PTS815 SJM 250 SMTR LFS_CNK, F.Cu at (40.9, 38.4)
- added SW3: BOOT_SW, OPI_CM5_PUSH_SW:SW4_PTS815 SJM 250 SMTR LFS_CNK, F.Cu at (40.9, 51.1)
- added SW4: PWR_SW, OPI_CM5_PUSH_SW:SW4_PTS815 SJM 250 SMTR LFS_CNK, F.Cu at (40.9, 32.0)
- added U4: SM8103ADC, Package_TO_SOT_SMD:SOT-23-6_Handsoldering, F.Cu at (181.3, 36.8)
- added U5: SM8103ADC, Package_TO_SOT_SMD:SOT-23-6_Handsoldering, F.Cu at (264.4, 62.5)
- moved U1 189.6 mm to (72.6, 62.2)
- moved D33 129.1 mm to (45.9, 51.1), turned to -90 degrees
- moved D4 128.7 mm to (45.9, 44.7), turned to -90 degrees
- moved D17 127.0 mm to (45.9, 38.4), turned to -90 degrees
- moved D2 126.8 mm to (45.9, 32.0), turned to -90 degrees
- moved ED5 112.3 mm to (67.7, 65.9)
- moved ED6 112.3 mm to (67.7, 68.3)
- moved U2 85.0 mm to (248.6, 65.8)
- moved J5 24.2 mm to (158.7, 44.5)
- moved H1 11.3 mm to (239.7, 66.3)
- moved H2 11.3 mm to (191.7, 66.3)
- moved H3 11.3 mm to (191.7, 33.3)
- moved H4 11.3 mm to (239.7, 33.3)
- moved J1 11.3 mm to (218.2, 66.5)
- moved J2 11.3 mm to (218.2, 32.5)
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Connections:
- net /GPIO0_D4 renamed /POWER_KEY
- net /VBUS renamed +5V_3A
- J1 pad 24: /GPIO1_C0 -> /I2C3_SDA_M0
- J1 pad 26: /GPIO1_C1 -> /I2C3_SCL_M0
- J1 pad 41: /GPIO1_B6 -> /I2C5_SCL_M3
- J1 pad 45: /GPIO1_B7 -> /I2C5_SDA_M3
- J1 pad 78: /GPIO_VREF -> /VCC_3V3_S3
- J1 pad 93: /SARADC_IN0 -> /BOOT_KEY
- J1 pad 95: /GPIO4_B6 -> /USER_KEY
- J3 pad 57: /GMAC_MCLK/PWM13 -> /GMAC_MCLK
- J3 pad 77: /GPIO0_D5 -> /USER_LED
- J3 pad 79: /GPIO0_C7 -> /DEBUG_LED
- J3 pad 83: /GPIO0_C4 -> /TMP_SN1_LED
- J3 pad 85: /GPIO0_D3 -> /TMP_SN2_LED
- J4 pad A1: unconnected-(J4-~{PRSNT1}-PadA1) -> +12V
- J4 pad A10: Net-(J4-+3.3V-PadA10) -> /+1.8V
- J4 pad A11: unconnected-(J4-~{PERST}-PadA11) -> /PMIC_RESET_L
- J4 pad A12: Net-(J4-GND-PadA12) -> unconnected-(J4-PadA12)
- J4 pad A14: unconnected-(J4-REFCLK--PadA14) -> GND
- J4 pad A15: Net-(J4-GND-PadA12) -> unconnected-(J4-PadA15)
- J4 pad A16: unconnected-(J4-PERp0-PadA16) -> /GMAC_MDC
- J4 pad A17: unconnected-(J4-PERn0-PadA17) -> /GMAC_TXCLK
- J4 pad A18: Net-(J4-GND-PadA12) -> /GMAC_RXD0
- J4 pad A19: unconnected-(J4-RSVD-PadA19) -> /GMAC_RXCLK
- J4 pad A2: Net-(J4-+12V-PadA2) -> +12V
- J4 pad A20: Net-(J4-GND-PadA12) -> /GMAC_RXD1
- J4 pad A21: unconnected-(J4-PERp1-PadA21) -> /GMAC_TXD0
- J4 pad A22: unconnected-(J4-PERn1-PadA22) -> /GMAC_TXD3
- J4 pad A23: Net-(J4-GND-PadA12) -> /GMAC_TXD2
- J4 pad A24: Net-(J4-GND-PadA12) -> /GMAC_TXD1
- J4 pad A25: unconnected-(J4-PERp2-PadA25) -> /GMAC_TXEN
- J4 pad A26: unconnected-(J4-PERn2-PadA26) -> /GMAC_MDIO
- J4 pad A27: Net-(J4-GND-PadA12) -> /GMAC_MCLK
- J4 pad A28: Net-(J4-GND-PadA12) -> /GMAC_RXDV
- J4 pad A29: unconnected-(J4-PERp3-PadA29) -> /GMAC_RXD2
- J4 pad A3: Net-(J4-+12V-PadA2) -> +12V
- J4 pad A30: unconnected-(J4-PERn3-PadA30) -> /GMAC_RXD3
- J4 pad A31: Net-(J4-GND-PadA12) -> unconnected-(J4-PadA31)
- J4 pad A4: Net-(J4-GND-PadA12) -> GND
- J4 pad A5: unconnected-(J4-JTAG2-PadA5) -> /+5V
- J4 pad A6: unconnected-(J4-JTAG3-PadA6) -> /+5V
- J4 pad A7: unconnected-(J4-JTAG4-PadA7) -> GND
- J4 pad A8: unconnected-(J4-JTAG5-PadA8) -> /+3.3V
- J4 pad A9: Net-(J4-+3.3V-PadA10) -> GND
- J4 pad B1: Net-(J4-+12V-PadA2) -> +12V
- J4 pad B10: unconnected-(J4-3.3Vaux-PadB10) -> /+1.8V
- J4 pad B11: unconnected-(J4-~{WAKE}-PadB11) -> /PWRON_L
- J4 pad B12: unconnected-(J4-RSVD-PadB12) -> /UART_TX
- J4 pad B13: Net-(J4-GND-PadA12) -> /UART_RX
- J4 pad B14: /USB20_HOST1_DP -> GND
- J4 pad B15: /USB20_HOST1_DN -> /USB20_HOST1_DM
- J4 pad B16: Net-(J4-GND-PadA12) -> /USB20_HOST1_DP
- J4 pad B17: unconnected-(J4-~{PRSNT2}-PadB17) -> GND
- J4 pad B18: Net-(J4-GND-PadA12) -> /HDMI0_TX_ON_H
- J4 pad B19: unconnected-(J4-PETp1-PadB19) -> /HDMI_TX0_CEC_M0
- J4 pad B2: Net-(J4-+12V-PadA2) -> +12V
- J4 pad B20: unconnected-(J4-PETn1-PadB20) -> /HDMI_TX0_SBDN
- J4 pad B21: Net-(J4-GND-PadA12) -> /HDMI_TX0_SDA_M0
- J4 pad B22: Net-(J4-GND-PadA12) -> /HDMI_TX0_D2P
- J4 pad B23: unconnected-(J4-PETp2-PadB23) -> /HDMI_TX0_D2N
- J4 pad B24: unconnected-(J4-PETn2-PadB24) -> /HDMI_TX0_D1P
- J4 pad B25: Net-(J4-GND-PadA12) -> /HDMI0_TX1N
- J4 pad B26: Net-(J4-GND-PadA12) -> /HDMI_TX0_SCL_M0
- J4 pad B27: unconnected-(J4-PETp3-PadB27) -> /HDMI_TX0_D3N
- J4 pad B28: unconnected-(J4-PETn3-PadB28) -> /HDMI_TX0_D3P
- J4 pad B29: Net-(J4-GND-PadA12) -> /HDMI_TX0_D0N
- J4 pad B3: Net-(J4-+12V-PadA2) -> +12V
- J4 pad B30: unconnected-(J4-RSVD-PadB30) -> /HDMI_TX0_D0P
- J4 pad B32: Net-(J4-GND-PadA12) -> /HDMI0_SBDP
- J4 pad B4: Net-(J4-GND-PadA12) -> GND
- J4 pad B5: unconnected-(J4-SMCLK-PadB5) -> /+5V
- J4 pad B6: unconnected-(J4-SMDAT-PadB6) -> /+5V
- J4 pad B7: Net-(J4-GND-PadA12) -> GND
- J4 pad B8: Net-(J4-+3.3V-PadA10) -> /+3.3V
- J4 pad B9: unconnected-(J4-JTAG1-PadB9) -> GND
- J5 pad 1: unconnected-(J5-CONFIG_3-Pad1) -> GND
- J5 pad 10: unconnected-(J5-DAS/DSS-Pad10) -> /M.2_ACT
- J5 pad 12: unconnected-(J5-VCC_3.3-Pad12) -> +3.3V_3A
- J5 pad 14: unconnected-(J5-VCC_3.3-Pad14) -> +3.3V_3A
- J5 pad 15: unconnected-(J5-GND-Pad15) -> GND
- J5 pad 16: unconnected-(J5-VCC_3.3-Pad16) -> +3.3V_3A
- J5 pad 18: unconnected-(J5-VCC_3.3-Pad18) -> +3.3V_3A
- J5 pad 2: unconnected-(J5-VCC_3.3-Pad2) -> +3.3V_3A
- J5 pad 21: unconnected-(J5-CONFIG_0-Pad21) -> GND
- J5 pad 27: unconnected-(J5-GND-Pad27) -> GND
- J5 pad 3: unconnected-(J5-GND-Pad3) -> GND
- J5 pad 33: unconnected-(J5-GND-Pad33) -> GND
- J5 pad 39: unconnected-(J5-GND-Pad39) -> GND
- J5 pad 4: unconnected-(J5-VCC_3.3-Pad4) -> +3.3V_3A
- J5 pad 41: unconnected-(J5-SATA_B+/PERN0-Pad41) -> /PCIE20_0_RXN
- J5 pad 43: unconnected-(J5-SATA_B-/PERP0-Pad43) -> /PCIE20_0_RXP
- J5 pad 45: unconnected-(J5-GND-Pad45) -> GND
- J5 pad 47: unconnected-(J5-SATA_A-/PETN0-Pad47) -> Net-(J5-SATA_A-/PETN0)
- J5 pad 49: unconnected-(J5-SATA_A+/PETP0-Pad49) -> Net-(J5-SATA_A+/PETP0)
- J5 pad 50: unconnected-(J5-~{PERST}-Pad50) -> /PCIE20x1_2_PERSTn_M0
- J5 pad 51: unconnected-(J5-GND-Pad51) -> GND
- J5 pad 52: unconnected-(J5-~{CLKREQ}-Pad52) -> /PCIE20x1_2_CLKREQn_M0
- J5 pad 53: unconnected-(J5-REFCLKN-Pad53) -> /PCIE20_0_REFCLKN
- J5 pad 54: unconnected-(J5-~{PEWAKE}-Pad54) -> /PCIE20x1_2_WAKEn_M0
- J5 pad 55: unconnected-(J5-REFCLKP-Pad55) -> /PCIE20_0_REFCLKP
- J5 pad 57: Net-(J5-GND-Pad57) -> GND
- J5 pad 69: unconnected-(J5-CONFIG_1-Pad69) -> GND
- J5 pad 70: unconnected-(J5-VCC_3.3-Pad70) -> +3.3V_3A
- J5 pad 71: unconnected-(J5-GND-Pad71) -> GND
- J5 pad 72: unconnected-(J5-VCC_3.3-Pad72) -> +3.3V_3A
- J5 pad 73: unconnected-(J5-GND-Pad73) -> GND
- J5 pad 74: unconnected-(J5-VCC_3.3-Pad74) -> +3.3V_3A
- J5 pad 75: unconnected-(J5-CONFIG_2-Pad75) -> GND
- J5 pad 80: unconnected-(J5-GND-Pad80) -> GND
- J5 pad 9: unconnected-(J5-GND-Pad9) -> GND
- J5 pad S1: Net-(J5-GND-Pad57) -> GND
- J5 pad S2: Net-(J5-GND-Pad57) -> GND
- U1 pad 1: unconnected-(U1-SDA-Pad1) -> /I2C5_SDA_M3
- U1 pad 2: unconnected-(U1-SCL-Pad2) -> /I2C5_SCL_M3
- U1 pad 3: unconnected-(U1-VDD-Pad3) -> +3.3V_3A
- U1 pad 4: unconnected-(U1-VSS-Pad4) -> GND
- U2 pad 1: unconnected-(U2-SDA-Pad1) -> /I2C3_SDA_M0
- U2 pad 2: unconnected-(U2-SCL-Pad2) -> /I2C3_SCL_M0
- U2 pad 3: unconnected-(U2-VDD-Pad3) -> +3.3V_3A
- U2 pad 4: unconnected-(U2-VSS-Pad4) -> GND
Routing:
- net +5V_3A: track 0.00 -> 58.9 mm
- net /HDMI0_SBDP: track 46.8 -> 0.00 mm
- net /HDMI0_TX_ON_H: track 45.0 -> 0.00 mm
- net /HDMI_TX0_D3P: track 43.9 -> 0.00 mm
- net /HDMI_TX0_D3N: track 42.8 -> 0.00 mm
- net /HDMI_TX0_D0P: track 42.2 -> 0.00 mm
- net /HDMI_TX0_CEC_M0: track 41.7 -> 0.00 mm
- net /HDMI_TX0_SBDN: track 41.0 -> 0.00 mm
- net /HDMI_TX0_D0N: track 40.9 -> 0.00 mm
- net /HDMI_TX0_D2P: track 40.5 -> 0.00 mm
- net /HDMI_TX0_D2N: track 39.7 -> 0.00 mm
- net /HDMI_TX0_D1P: track 38.9 -> 0.00 mm
- net /HDMI_TX0_SCL_M0: track 38.2 -> 0.00 mm
- net /HDMI_TX0_D1N: track 38.1 -> 0.00 mm
- net /HDMI_TX0_SDA_M0: track 32.4 -> 0.00 mm
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- added copper zone on In1.Cu, net GND
- added copper zone on In2.Cu, net GND
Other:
- outline, holes or cut-outs redrawn
